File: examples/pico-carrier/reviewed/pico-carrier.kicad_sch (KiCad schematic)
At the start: 12 parts, among them J1 5V IN, J3 GP0-GP15, J4 GP16-GP28, PWR, U1 Pico

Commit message: Walk the whole edge for a screw hole, and land a joint on its own pad
The fastener clearance was right and the search was not: it slid along two
edges from each corner and gave up, so boards that had had four screw holes
came back with one. It now walks a ring round the board at the inset the
screw needs, taking the nearest free point to each corner - and only from
that corner's own quarter, because a search that asked for the nearest free
point anywhere put three of the four along one edge, each of them the nearest
thing to a different corner. A quarter with no room gives no screw: three
that hold the board flat beat four that hold one side.

A pin header asks for nothing above its courtyard - the socket that fits it
lands inside the outline the header already draws - while a screw terminal's
wires leave horizontally from its face. Treating the two alike is what left a
carrier lined with headers with two holes on one edge. Both the generator and
the rule now tell them apart by footprint.

_landed folds a via that sits beside a plated hole of its own net onto the
hole. The plating already joins the faces, so the via bought nothing and cost
hole-to-hole: two drills a millimetre apart leave 0.15 mm of laminate at a
0.25 mm rule, which is what DRC reported on the opamp board.

The fillets move to the end of the pipeline. A taper is built against the end
of a run, and _landed moves ends, so a teardrop laid before it pointed at
where the run used to stop - a nought-degree corner in the angle rule.

buck-5v, motor-driver, pico-carrier, opamp-filter: 0 errors, 0 warnings.

Co-Authored-By: Claude Fable 5 <noreply@anthropic.com>
Claude-Session: https://claude.ai/code/session_01DUj7Ltu92tWg159mCSacwY
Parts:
- added FID3: Fiducial, Fiducial:Fiducial_1mm_Mask2mm, symbol Mechanical:Fiducial
- added H2: M3, MountingHole:MountingHole_3.2mm_M3, symbol Mechanical:MountingHole
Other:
- moved on the sheet: FID1, FID2
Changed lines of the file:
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@@
     (instances (project "pico-carrier" (path "/f86b03a2-2f64-5dc5-a6a7-b575bc25ae3a" (reference "H1") (unit 1))))
   )
-  (symbol (lib_id "Mechanical:Fiducial") (at 114.3 149.86 0.0) (unit 1)
+  (symbol (lib_id "Mechanical:MountingHole") (at 114.3 149.86 0.0) (unit 1)
     (exclude_from_sim no) (in_bom no) (on_board yes) (dnp no)
-    (property "Reference" "FID1" (at 113.03 146.05 0) (effects (font (size 1.27 1.27)) (justify right)))
-    (property "Value" "Fiducial" (at 118.11 152.4 0) (effects (font (size 1.27 1.27)) (justify left) hide))
-    (property "Footprint" "Fiducial:Fiducial_1mm_Mask2mm" (at 114.3 149.86 0) (effects (font (size 1.27 1.27)) hide))
+    (property "Reference" "H2" (at 113.03 146.05 0) (effects (font (size 1.27 1.27)) (justify right)))
+    (property "Value" "M3" (at 118.11 152.4 0) (effects (font (size 1.27 1.27)) (justify left) hide))
+    (property "Footprint" "MountingHole:MountingHole_3.2mm_M3" (at 114.3 149.86 0) (effects (font (size 1.27 1.27)) hide))
     (property "Datasheet" "~" (at 114.3 149.86 0) (effects (font (size 1.27 1.27)) hide))
     (property "MPN" "n/a" (at 114.3 149.86 0) (effects (font (size 1.27 1.27)) hide))
     (property "Manufacturer" "n/a" (at 114.3 149.86 0) (effects (font (size 1.27 1.27)) hide))
+    (instances (project "pico-carrier" (path "/f86b03a2-2f64-5dc5-a6a7-b575bc25ae3a" (reference "H2") (unit 1))))
+  )
+  (symbol (lib_id "Mechanical:Fiducial") (at 228.6 149.86 0.0) (unit 1)
+    (exclude_from_sim no) (in_bom no) (on_board yes) (dnp no)
+    (property "Reference" "FID1" (at 227.33 146.05 0) (effects (font (size 1.27 1.27)) (justify right)))
+    (property "Value" "Fiducial" (at 232.41 152.4 0) (effects (font (size 1.27 1.27)) (justify left) hide))
+    (property "Footprint" "Fiducial:Fiducial_1mm_Mask2mm" (at 228.6 149.86 0) (effects (font (size 1.27 1.27)) hide))
+    (property "Datasheet" "~" (at 228.6 149.86 0) (effects (font (size 1.27 1.27)) hide))
+    (property "MPN" "n/a" (at 228.6 149.86 0) (effects (font (size 1.27 1.27)) hide))
+    (property "Manufacturer" "n/a" (at 228.6 149.86 0) (effects (font (size 1.27 1.27)) hide))
     (instances (project "pico-carrier" (path "/f86b03a2-2f64-5dc5-a6a7-b575bc25ae3a" (reference "FID1") (unit 1))))
   )
-  (symbol (lib_id "Mechanical:Fiducial") (at 127.0 149.86 0.0) (unit 1)
+  (symbol (lib_id "Mechanical:Fiducial") (at 241.29999999999998 149.86 0.0) (unit 1)
     (exclude_from_sim no) (in_bom no) (on_board yes) (dnp no)
-    (property "Reference" "FID2" (at 125.73 146.05 0) (effects (font (size 1.27 1.27)) (justify right)))
-    (property "Value" "Fiducial" (at 130.81 152.4 0) (effects (font (size 1.27 1.27)) (justify left) hide))
-    (property "Footprint" "Fiducial:Fiducial_1mm_Mask2mm" (at 127.0 149.86 0) (effects (font (size 1.27 1.27)) hide))
-    (property "Datasheet" "~" (at 127.0 149.86 0) (effects (font (size 1.27 1.27)) hide))
-    (property "MPN" "n/a" (at 127.0 149.86 0) (effects (font (size 1.27 1.27)) hide))
-    (property "Manufacturer" "n/a" (at 127.0 149.86 0) (effects (font (size 1.27 1.27)) hide))
+    (property "Reference" "FID2" (at 240.03 146.05 0) (effects (font (size 1.27 1.27)) (justify right)))
+    (property "Value" "Fiducial" (at 245.11 152.4 0) (effects (font (size 1.27 1.27)) (justify left) hide))
+    (property "Footprint" "Fiducial:Fiducial_1mm_Mask2mm" (at 241.29999999999998 149.86 0) (effects (font (size 1.27 1.27)) hide))
+    (property "Datasheet" "~" (at 241.29999999999998 149.86 0) (effects (font (size 1.27 1.27)) hide))
+    (property "MPN" "n/a" (at 241.29999999999998 149.86 0) (effects (font (size 1.27 1.27)) hide))
+    (property "Manufacturer" "n/a" (at 241.29999999999998 149.86 0) (effects (font (size 1.27 1.27)) hide))
     (instances (project "pico-carrier" (path "/f86b03a2-2f64-5dc5-a6a7-b575bc25ae3a" (reference "FID2") (unit 1))))
   )
+  (symbol (lib_id "Mechanical:Fiducial") (at 254.0 149.86 0.0) (unit 1)
+    (exclude_from_sim no) (in_bom no) (on_board yes) (dnp no)
+    (property "Reference" "FID3" (at 252.73 146.05 0) (effects (font (size 1.27 1.27)) (justify right)))
+    (property "Value" "Fiducial" (at 257.81 152.4 0) (effects (font (size 1.27 1.27)) (justify left) hide))
+    (property "Footprint" "Fiducial:Fiducial_1mm_Mask2mm" (at 254.0 149.86 0) (effects (font (size 1.27 1.27)) hide))
+    (property "Datasheet" "~" (at 254.0 149.86 0) (effects (font (size 1.27 1.27)) hide))
+    (property "MPN" "n/a" (at 254.0 149.86 0) (effects (font (size 1.27 1.27)) hide))
+    (property "Manufacturer" "n/a" (at 254.0 149.86 0) (effects (font (size 1.27 1.27)) hide))
+    (instances (project "pico-carrier" (path "/f86b03a2-2f64-5dc5-a6a7-b575bc25ae3a" (reference "FID3") (unit 1))))
+  )
   (wire (pts (xy 180.34 107.95) (xy 180.34 105.41)) (stroke (width 0) (type default)))

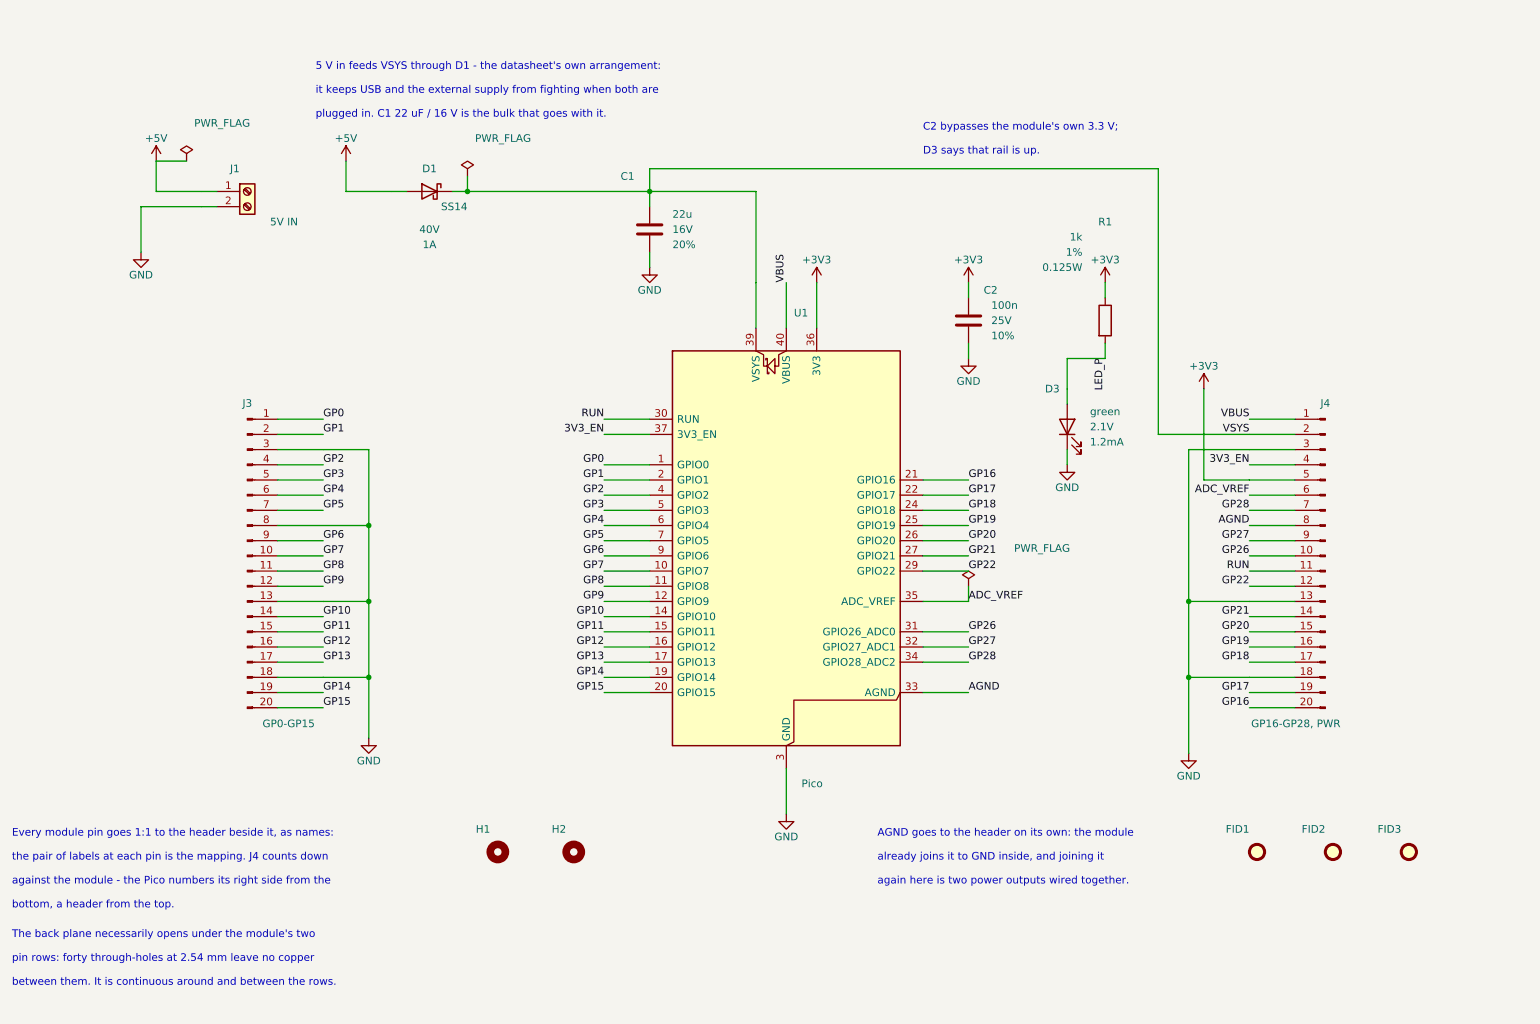
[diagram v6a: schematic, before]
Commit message: feat(examples): round twenty - fuse and clamp every input, state the ESR, damp the clock, control the mute
Redesign of the five worked examples for the items REVIEW.md left open:

- every power input gets a fuse in series and a TVS across the fused rail
  (a resettable fuse on the Pico carrier, whose Schottky already blocks a
  reversed supply); each sheet states what the clamp does not do
- the buck's output capacitor states the ESR the LM2596 loop is designed
  around (SNVS124G 9.1.3), derived from the ripple already on the sheet
- the FPGA's 12 MHz clock leaves its oscillator through 33 ohms
- the DAC's XSMT is driven from the FPGA with a pull-down instead of
  strapped high, so it comes up muted
- the op-amp filter's output goes through a 100 ohm isolation resistor

Generator fixes the round found: _surfaced pruned a via that tapped the
middle of a back-layer spine, and _chamfer_tracks cut the copper out from
under a via sitting a fraction along a leg; both left a net in two pieces
that KiCad's DRC reported. Pin stubs closer than 7.62 mm draw over each
other, so the new parts are spaced for it and the comments say why.

tools/example_images.py renders the README pictures from the regenerated
projects. All five reviewed variants pass their gates and KiCad's DRC on
both matrix versions; the as-generated variants each carry one more
blocking finding (spec.missing_esr). REVIEW.md 25 records the round.

Co-Authored-By: Claude Fable 5.1 <noreply@anthropic.com>
Claude-Session: https://claude.ai/code/session_017JKofiLFxXjzRRnBmFyXuQ
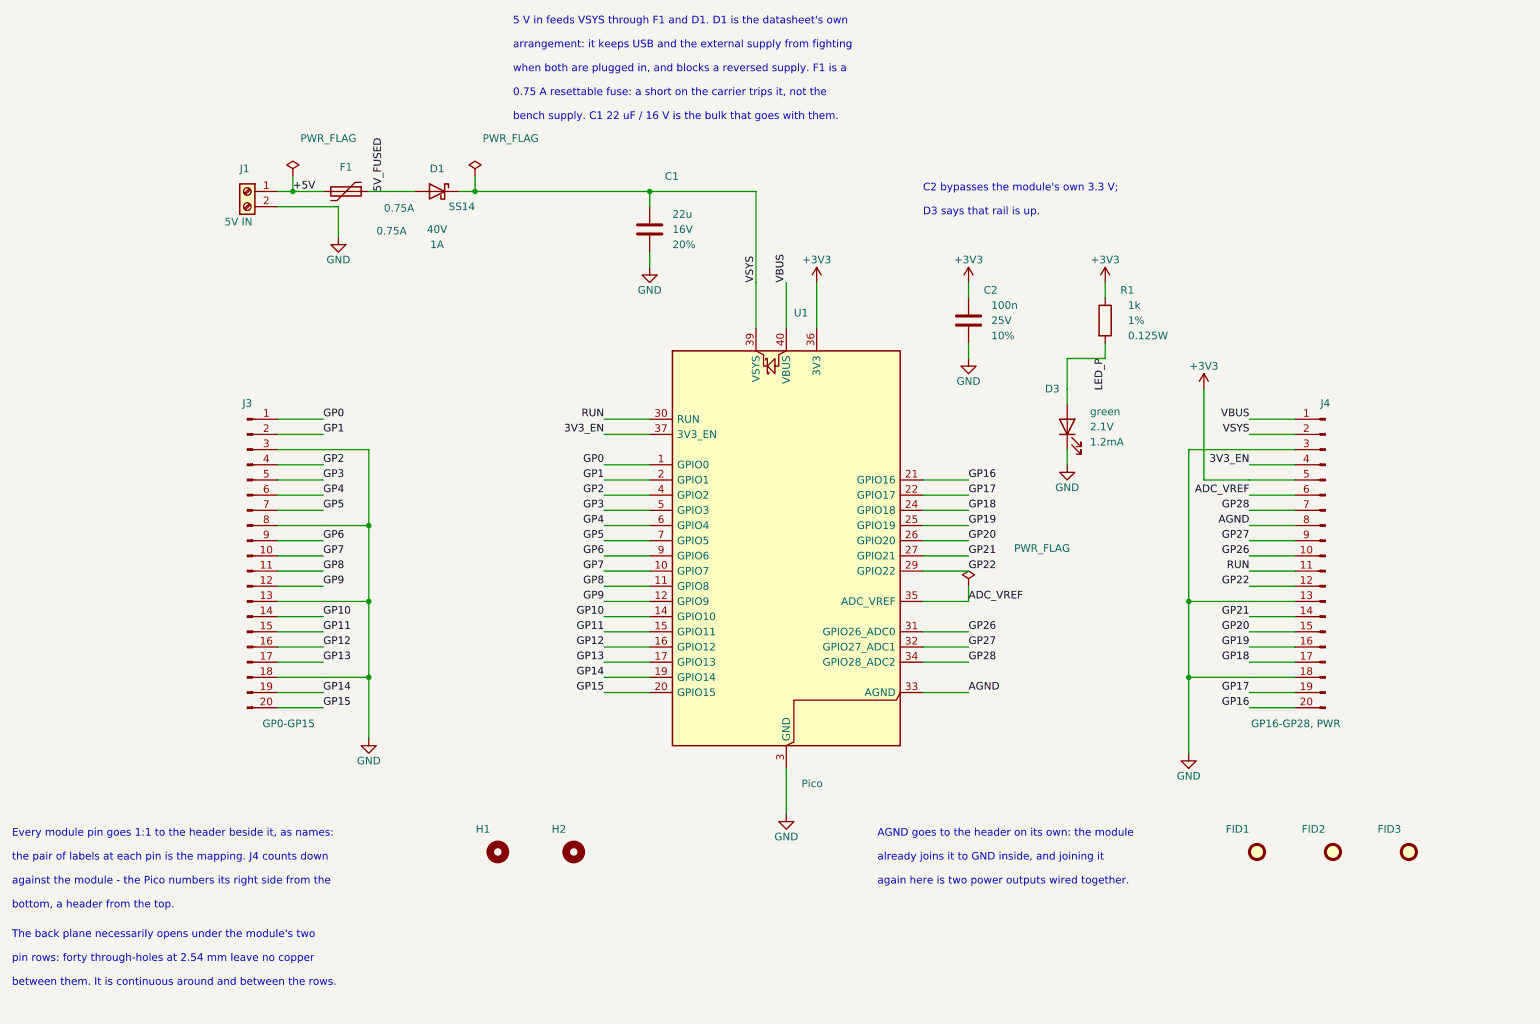
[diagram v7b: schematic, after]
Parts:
- added F1: 0.75A, Fuse:Fuse_1812_4532Metric, symbol Device:Polyfuse
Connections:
- net +5V: now also F1.2; no longer D1.2 (A)
- new net 5V_FUSED: D1.2 (A), F1.1
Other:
- note added: "0.75 A resettable fuse: a short on the carrier trips it, not the"
- note added: "5 V in feeds VSYS through F1 and D1. D1 is the datasheet's own"
- note added: "arrangement: it keeps USB and the external supply from fighting"
- note added: "bench supply. C1 22 uF / 16 V is the bulk that goes with them."
- note added: "when both are plugged in, and blocks a reversed supply. F1 is a"
- note removed: "5 V in feeds VSYS through D1 - the datasheet's own arrangement:"
- note removed: "it keeps USB and the external supply from fighting when both are"
- note removed: "plugged in. C1 22 uF / 16 V is the bulk that goes with it."
- moved on the sheet: D1, J1
